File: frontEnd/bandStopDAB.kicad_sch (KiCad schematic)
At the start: 18 parts, among them U401 BGS12P2L6E6327XTSA1, U402 BGS12P2L6E6327XTSA1

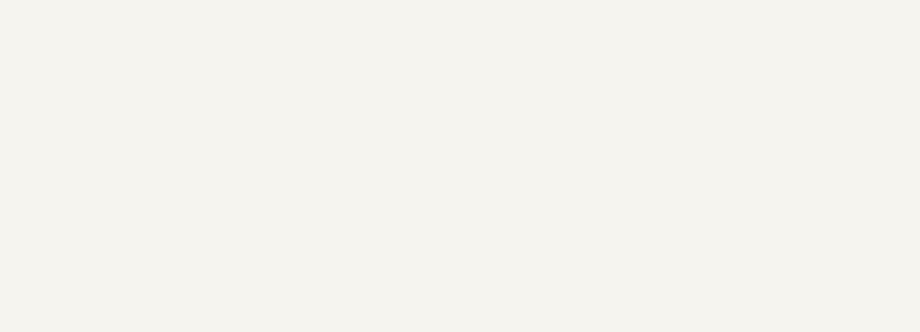
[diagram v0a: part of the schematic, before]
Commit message: update schematics, add bypass for the attenuator
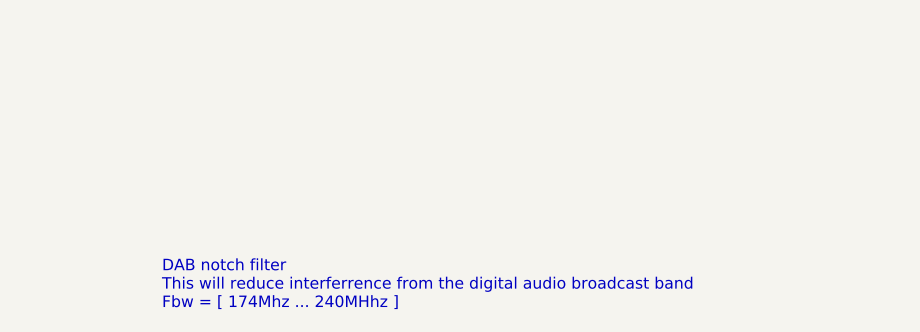
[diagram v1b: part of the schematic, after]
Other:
- note added: "DAB notch filter This will reduce interferrence from the digital audio broadcast band Fbw = [ 174Mhz ... 240MHhz ]"
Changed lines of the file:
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@@
     (stroke (width 0) (type default) (color 0 0 0 0))
+  )
+  (text "DAB notch filter\nThis will reduce interferrence from the digital audio broadcast band\nFbw = [ 174Mhz ... 240MHhz ]"
+    (at 180.34 176.53 0)
+    (effects (font (size 1.27 1.27)) (justify left bottom))
   )
   (hierarchical_label "RF_OUT" (shape output) (at 248.92 77.47 0)

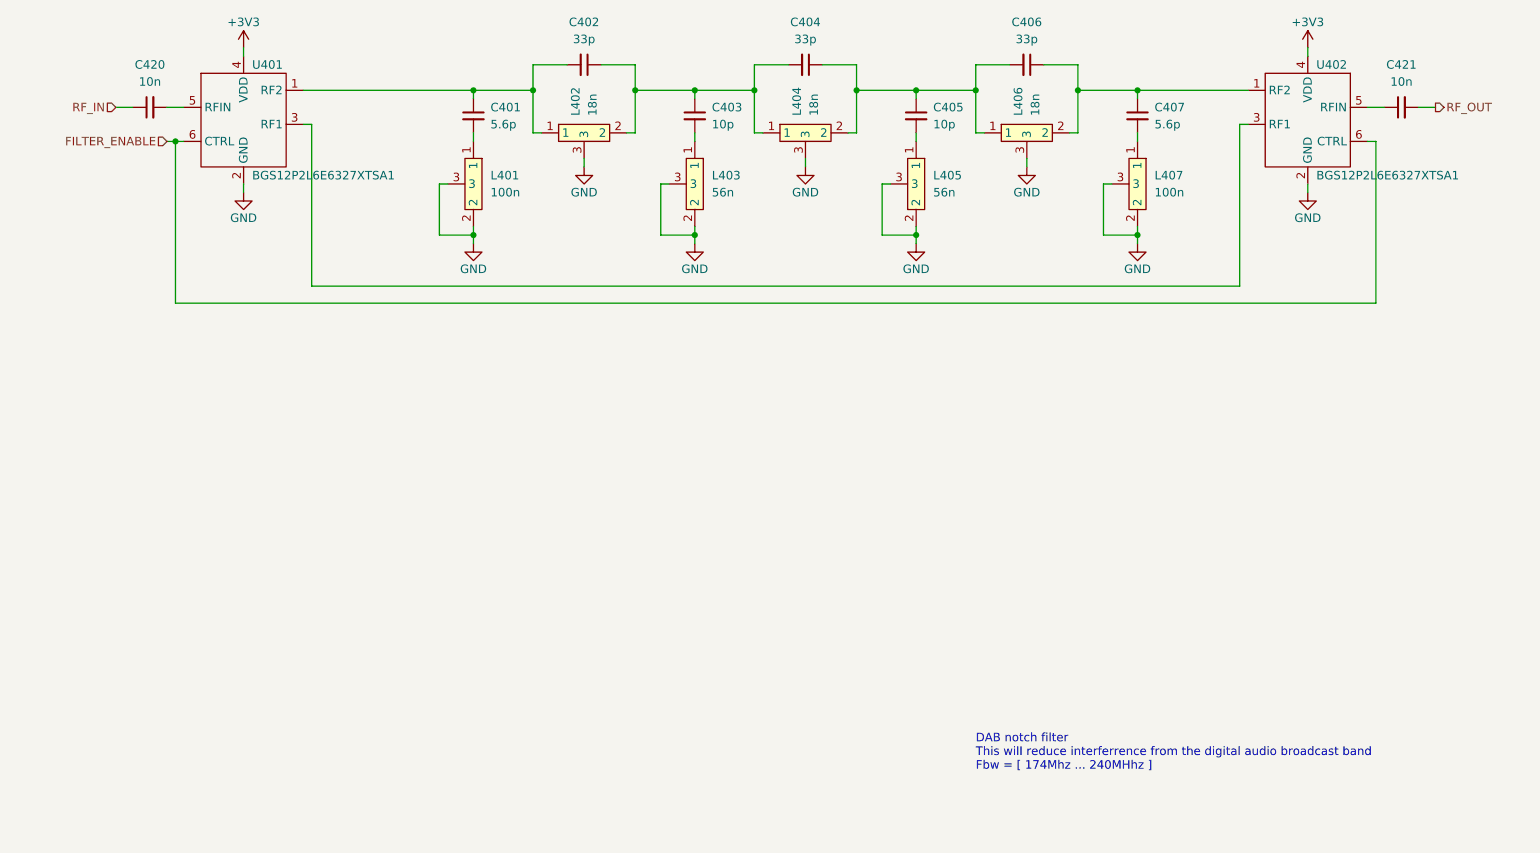
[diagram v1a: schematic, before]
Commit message: simply schematic: remove attenuator and gain blocks; add 5 way multiplexer
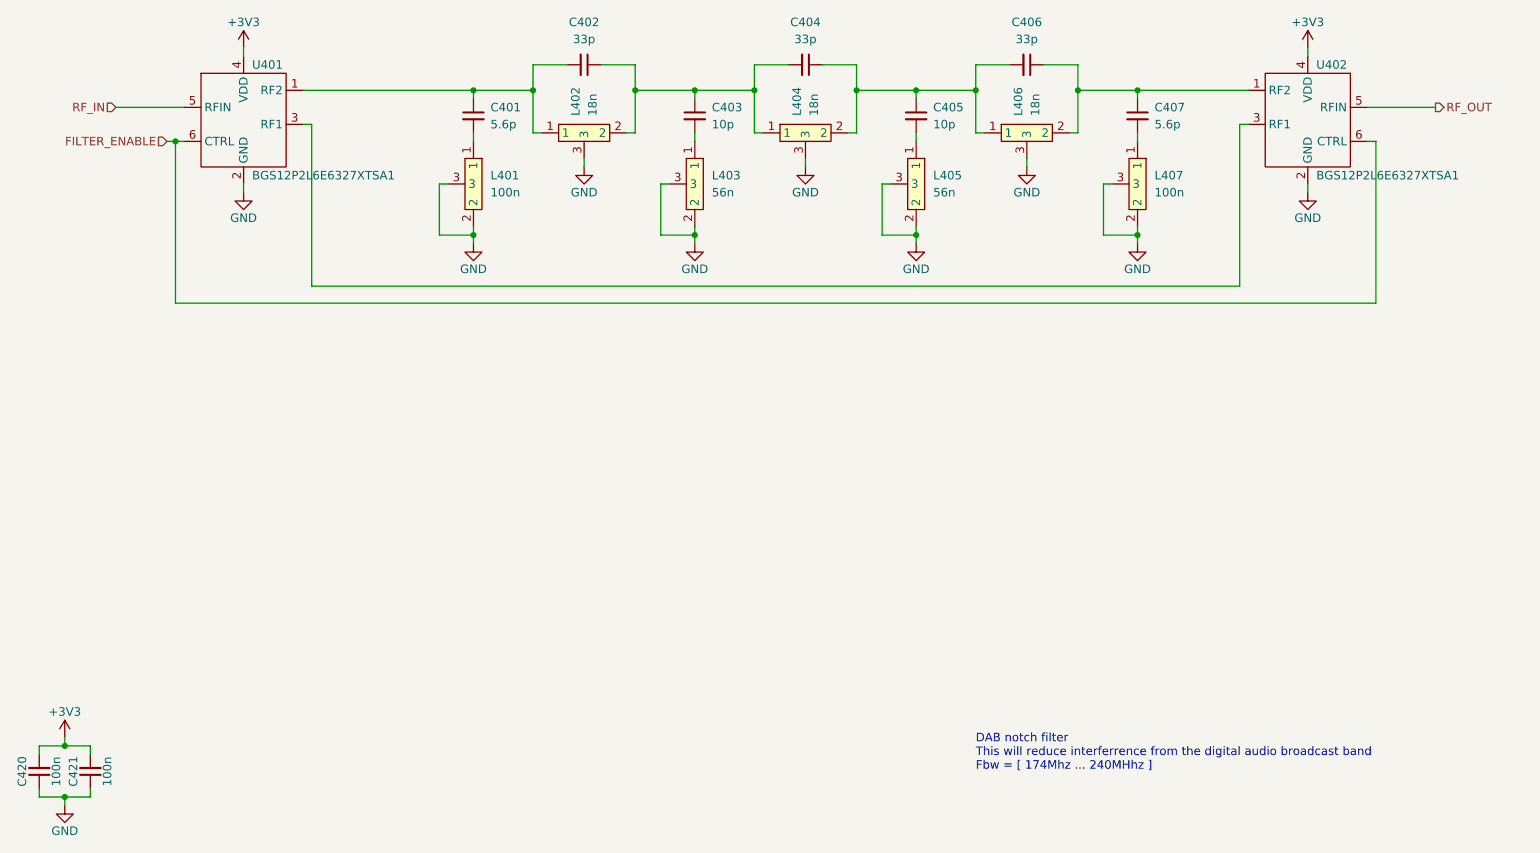
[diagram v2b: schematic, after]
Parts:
- C420, C421: value 10n -> 100n
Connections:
- net +3V3: now also C420.2, C421.2
- net GND: now also C420.1, C421.1
- net RF_IN: now also U401.5 (RFIN); no longer C420.1
- net RF_OUT: now also U402.5 (RFIN); no longer C421.2
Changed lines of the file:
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@@
   (junction (at 180.34 74.93) (diameter 0) (color 0 0 0 0)
   )
+  (junction (at 44.45 180.34) (diameter 0) (color 0 0 0 0)
+  )
   (junction (at 60.96 82.55) (diameter 0) (color 0 0 0 0)
   )
@@
   (junction (at 147.32 74.93) (diameter 0) (color 0 0 0 0)
   )
+  (junction (at 44.45 172.72) (diameter 0) (color 0 0 0 0)
+  )
   (junction (at 204.47 96.52) (diameter 0) (color 0 0 0 0)
   )
@@
   (junction (at 171.45 74.93) (diameter 0) (color 0 0 0 0)
   )
+  (wire (pts (xy 44.45 172.72) (xy 48.26 172.72))
+    (stroke (width 0) (type default) (color 0 0 0 0))
+  )
   (wire (pts (xy 229.87 68.58) (xy 229.87 69.85))
     (stroke (width 0) (type default) (color 0 0 0 0))
@@
     (stroke (width 0) (type default) (color 0 0 0 0))
   )
-  (wire (pts (xy 238.76 77.47) (xy 241.3 77.47))
-    (stroke (width 0) (type default) (color 0 0 0 0))
-  )
   (wire (pts (xy 100.33 96.52) (xy 105.41 96.52))
     (stroke (width 0) (type default) (color 0 0 0 0))
   )
+  (wire (pts (xy 48.26 179.07) (xy 48.26 180.34))
+    (stroke (width 0) (type default) (color 0 0 0 0))
+  )
   (wire (pts (xy 162.56 81.28) (xy 162.56 74.93))
     (stroke (width 0) (type default) (color 0 0 0 0))
@@
     (stroke (width 0) (type default) (color 0 0 0 0))
   )
+  (wire (pts (xy 40.64 173.99) (xy 40.64 172.72))
+    (stroke (width 0) (type default) (color 0 0 0 0))
+  )
   (wire (pts (xy 166.37 88.9) (xy 166.37 96.52))
     (stroke (width 0) (type default) (color 0 0 0 0))
@@
     (stroke (width 0) (type default) (color 0 0 0 0))
   )
+  (wire (pts (xy 44.45 180.34) (xy 48.26 180.34))
+    (stroke (width 0) (type default) (color 0 0 0 0))
+  )
   (wire (pts (xy 114.3 74.93) (xy 105.41 74.93))
     (stroke (width 0) (type default) (color 0 0 0 0))
   )
+  (wire (pts (xy 40.64 180.34) (xy 44.45 180.34))
+    (stroke (width 0) (type default) (color 0 0 0 0))
+  )
   (wire (pts (xy 134.62 88.9) (xy 133.35 88.9))
     (stroke (width 0) (type default) (color 0 0 0 0))
@@
     (stroke (width 0) (type default) (color 0 0 0 0))
   )
+  (wire (pts (xy 44.45 180.34) (xy 44.45 181.61))
+    (stroke (width 0) (type default) (color 0 0 0 0))
+  )
   (wire (pts (xy 238.76 82.55) (xy 240.03 82.55))
     (stroke (width 0) (type default) (color 0 0 0 0))
@@
     (stroke (width 0) (type default) (color 0 0 0 0))
   )
+  (wire (pts (xy 40.64 179.07) (xy 40.64 180.34))
+    (stroke (width 0) (type default) (color 0 0 0 0))
+  )
   (wire (pts (xy 71.12 88.9) (xy 71.12 90.17))
     (stroke (width 0) (type default) (color 0 0 0 0))
@@
     (stroke (width 0) (type default) (color 0 0 0 0))
   )
-  (wire (pts (xy 246.38 77.47) (xy 248.92 77.47))
+  (wire (pts (xy 238.76 77.47) (xy 248.92 77.47))
     (stroke (width 0) (type default) (color 0 0 0 0))
   )
@@
     (stroke (width 0) (type default) (color 0 0 0 0))
   )
-  (wire (pts (xy 52.07 77.47) (xy 54.61 77.47))
-    (stroke (width 0) (type default) (color 0 0 0 0))
-  )
   (wire (pts (xy 195.58 71.12) (xy 195.58 74.93))
     (stroke (width 0) (type default) (color 0 0 0 0))
@@
     (stroke (width 0) (type default) (color 0 0 0 0))
   )
-  (wire (pts (xy 59.69 77.47) (xy 62.23 77.47))
+  (wire (pts (xy 52.07 77.47) (xy 62.23 77.47))
     (stroke (width 0) (type default) (color 0 0 0 0))
   )
@@
     (stroke (width 0) (type default) (color 0 0 0 0))
   )
+  (wire (pts (xy 48.26 172.72) (xy 48.26 173.99))
+    (stroke (width 0) (type default) (color 0 0 0 0))
+  )
   (wire (pts (xy 147.32 81.28) (xy 148.59 81.28))
     (stroke (width 0) (type default) (color 0 0 0 0))
@@
     (stroke (width 0) (type default) (color 0 0 0 0))
   )
+  (wire (pts (xy 40.64 172.72) (xy 44.45 172.72))
+    (stroke (width 0) (type default) (color 0 0 0 0))
+  )
   (wire (pts (xy 240.03 82.55) (xy 240.03 106.68))
+    (stroke (width 0) (type default) (color 0 0 0 0))
+  )
+  (wire (pts (xy 44.45 171.45) (xy 44.45 172.72))
     (stroke (width 0) (type default) (color 0 0 0 0))
   )
@@
     (effects (font (size 1.27 1.27)) (justify right))
   )
+  (symbol (lib_id "Device:C_Small") (at 40.64 176.53 180) (unit 1)
+    (in_bom yes) (on_board yes)
+    (property "Reference" "C420" (id 0) (at 38.1 176.53 90))
+    (property "Value" "100n" (id 1) (at 43.18 176.53 90))
+    (property "Footprint" "Capacitor_SMD:C_0805_2012Metric" (id 2) (at 40.64 176.53 0)
+      (effects (font (size 1.27 1.27)) hide)
+    )
+    (property "Datasheet" "~" (id 3) (at 40.64 176.53 0)
+      (effects (font (size 1.27 1.27)) hide)
+    )
+    (pin "1")
+    (pin "2")
+  )
   (symbol (lib_id "frontEnd:DIY_COIL") (at 154.94 81.28 0) (unit 1)
     (in_bom yes) (on_board yes)
@@
     (pin "1")
   )
+  (symbol (lib_id "power:+3V3") (at 44.45 171.45 0) (unit 1)
+    (in_bom yes) (on_board yes)
+    (property "Reference" "#PWR?" (id 0) (at 44.45 175.26 0)
+      (effects (font (size 1.27 1.27)) hide)
+    )
+    (property "Value" "+3V3" (id 1) (at 44.45 167.64 0))
+    (property "Footprint" "" (id 2) (at 44.45 171.45 0)
+      (effects (font (size 1.27 1.27)) hide)
+    )
+    (property "Datasheet" "" (id 3) (at 44.45 171.45 0)
+      (effects (font (size 1.27 1.27)) hide)
+    )
+    (pin "1")
+  )
   (symbol (lib_id "power:GND") (at 171.45 97.79 0) (unit 1)
     (in_bom yes) (on_board yes)
@@
     )
     (property "Datasheet" "" (id 3) (at 171.45 97.79 0)
+      (effects (font (size 1.27 1.27)) hide)
+    )
+    (pin "1")
+  )
+  (symbol (lib_id "power:GND") (at 44.45 181.61 0) (unit 1)
+    (in_bom yes) (on_board yes)
+    (property "Reference" "#PWR?" (id 0) (at 44.45 187.96 0)
+      (effects (font (size 1.27 1.27)) hide)
+    )
+    (property "Value" "GND" (id 1) (at 44.45 185.42 0))
+    (property "Footprint" "" (id 2) (at 44.45 181.61 0)
+      (effects (font (size 1.27 1.27)) hide)
+    )
+    (property "Datasheet" "" (id 3) (at 44.45 181.61 0)
       (effects (font (size 1.27 1.27)) hide)
     )
@@
     (pin "6")
   )
-  (symbol (lib_id "Device:C_Small") (at 57.15 77.47 90) (unit 1)
-    (in_bom yes) (on_board yes) (fields_autoplaced)
-    (property "Reference" "C420" (id 0) (at 57.1563 71.12 90))
-    (property "Value" "10n" (id 1) (at 57.1563 73.66 90))
-    (property "Footprint" "Capacitor_SMD:C_0805_2012Metric" (id 2) (at 57.15 77.47 0)
-      (effects (font (size 1.27 1.27)) hide)
-    )
-    (property "Datasheet" "~" (id 3) (at 57.15 77.47 0)
+  (symbol (lib_id "Device:C_Small") (at 48.26 176.53 180) (unit 1)
+    (in_bom yes) (on_board yes)
+    (property "Reference" "C421" (id 0) (at 45.72 176.53 90))
+    (property "Value" "100n" (id 1) (at 50.8 176.53 90))
+    (property "Footprint" "Capacitor_SMD:C_0805_2012Metric" (id 2) (at 48.26 176.53 0)
+      (effects (font (size 1.27 1.27)) hide)
+    )
+    (property "Datasheet" "~" (id 3) (at 48.26 176.53 0)
       (effects (font (size 1.27 1.27)) hide)
     )
@@
     (pin "3")
   )
-  (symbol (lib_id "Device:C_Small") (at 243.84 77.47 90) (unit 1)
-    (in_bom yes) (on_board yes) (fields_autoplaced)
-    (property "Reference" "C421" (id 0) (at 243.8463 71.12 90))
-    (property "Value" "10n" (id 1) (at 243.8463 73.66 90))
-    (property "Footprint" "Capacitor_SMD:C_0805_2012Metric" (id 2) (at 243.84 77.47 0)
-      (effects (font (size 1.27 1.27)) hide)
-    )
-    (property "Datasheet" "~" (id 3) (at 243.84 77.47 0)
-      (effects (font (size 1.27 1.27)) hide)
-    )
-    (pin "1")
-    (pin "2")
-  )
   (symbol (lib_id "Device:C_Small") (at 187.96 71.12 270) (unit 1)
